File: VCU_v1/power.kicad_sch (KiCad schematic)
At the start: 0 parts

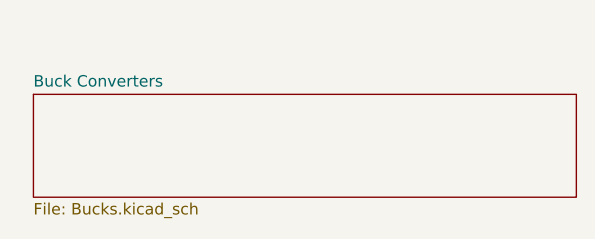
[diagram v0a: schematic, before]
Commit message: finished 12-5 buck
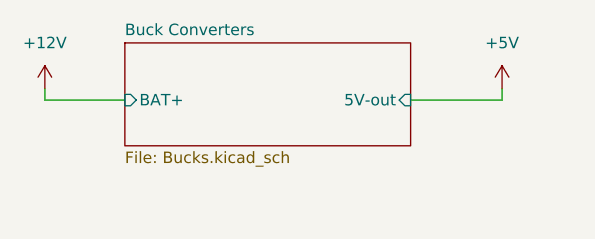
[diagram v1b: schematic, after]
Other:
- sheet Buck Converters ports: added 5V-out, BAT+; removed none
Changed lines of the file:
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@@
 	(generator_version "9.0")
 	(paper "A4")
-	(sheet
-		(at 102.87 51.435)
-		(size 60.325 11.43)
+	(wire
+		(pts
+			(xy 154.94 52.07) (xy 154.94 50.8)
+		)
+		(stroke
+			(width 0)
+			(type default)
+		)
+	)
+	(wire
+		(pts
+			(xy 144.78 52.07) (xy 154.94 52.07)
+		)
+		(stroke
+			(width 0)
+			(type default)
+		)
+	)
+	(wire
+		(pts
+			(xy 104.14 52.07) (xy 113.03 52.07)
+		)
+		(stroke
+			(width 0)
+			(type default)
+		)
+	)
+	(wire
+		(pts
+			(xy 104.14 50.8) (xy 104.14 52.07)
+		)
+		(stroke
+			(width 0)
+			(type default)
+		)
+	)
+	(symbol
+		(lib_id "power:+12V")
+		(at 104.14 50.8 0)
+		(unit 1)
 		(exclude_from_sim no)
 		(in_bom yes)
@@
 		(dnp no)
 		(fields_autoplaced yes)
+		(property "Reference" "#PWR09"
+			(at 104.14 54.61 0)
+			(effects
+				(font
+					(size 1.27 1.27)
+				)
+				(hide yes)
+			)
+		)
+		(property "Value" "+12V"
+			(at 104.14 45.72 0)
+			(effects
+				(font
+					(size 1.27 1.27)
+				)
+			)
+		)
+		(property "Footprint" ""
+			(at 104.14 50.8 0)
+			(effects
+				(font
+					(size 1.27 1.27)
+				)
+				(hide yes)
+			)
+		)
+		(property "Datasheet" ""
+			(at 104.14 50.8 0)
+			(effects
+				(font
+					(size 1.27 1.27)
+				)
+				(hide yes)
+			)
+		)
+		(property "Description" "Power symbol creates a global label with name \"+12V\""
+			(at 104.14 50.8 0)
+			(effects
+				(font
+					(size 1.27 1.27)
+				)
+				(hide yes)
+			)
+		)
+		(pin "1"
+		)
+		(instances
+			(project ""
+				(path "/4ee6c2ad-9a1b-4276-b3cf-1cc8dc52967e/9e4b5f8d-93dc-46d5-aa92-d0e0d2e07b3d"
+					(reference "#PWR09")
+					(unit 1)
+				)
+			)
+		)
+	)
+	(symbol
+		(lib_id "power:+5V")
+		(at 154.94 50.8 0)
+		(unit 1)
+		(exclude_from_sim no)
+		(in_bom yes)
+		(on_board yes)
+		(dnp no)
+		(fields_autoplaced yes)
+		(property "Reference" "#PWR010"
+			(at 154.94 54.61 0)
+			(effects
+				(font
+					(size 1.27 1.27)
+				)
+				(hide yes)
+			)
+		)
+		(property "Value" "+5V"
+			(at 154.94 45.72 0)
+			(effects
+				(font
+					(size 1.27 1.27)
+				)
+			)
+		)
+		(property "Footprint" ""
+			(at 154.94 50.8 0)
+			(effects
+				(font
+					(size 1.27 1.27)
+				)
+				(hide yes)
+			)
+		)
+		(property "Datasheet" ""
+			(at 154.94 50.8 0)
+			(effects
+				(font
+					(size 1.27 1.27)
+				)
+				(hide yes)
+			)
+		)
+		(property "Description" "Power symbol creates a global label with name \"+5V\""
+			(at 154.94 50.8 0)
+			(effects
+				(font
+					(size 1.27 1.27)
+				)
+				(hide yes)
+			)
+		)
+		(pin "1"
+		)
+		(instances
+			(project ""
+				(path "/4ee6c2ad-9a1b-4276-b3cf-1cc8dc52967e/9e4b5f8d-93dc-46d5-aa92-d0e0d2e07b3d"
+					(reference "#PWR010")
+					(unit 1)
+				)
+			)
+		)
+	)
+	(sheet
+		(at 113.03 45.72)
+		(size 31.75 11.43)
+		(exclude_from_sim no)
+		(in_bom yes)
+		(on_board yes)
+		(dnp no)
+		(fields_autoplaced yes)
 		(stroke
 			(width 0.1524)
@@
 		)
 		(property "Sheetname" "Buck Converters"
-			(at 102.87 50.7234 0)
+			(at 113.03 45.0084 0)
 			(effects
 				(font
@@
 		)
 		(property "Sheetfile" "Bucks.kicad_sch"
-			(at 102.87 63.4496 0)
+			(at 113.03 57.7346 0)
 			(effects
 				(font
@@
 			)
 		)
+		(pin "BAT+" input
+			(at 113.03 52.07 180)
+			(effects
+				(font
+					(size 1.27 1.27)
+				)
+				(justify left)
+			)
+		)
+		(pin "5V-out" input
+			(at 144.78 52.07 0)
+			(effects
+				(font
+					(size 1.27 1.27)
+				)
+				(justify right)
+			)
+		)

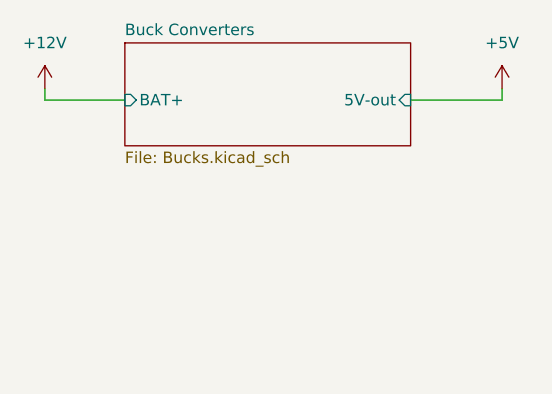
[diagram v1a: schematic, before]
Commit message: added STM, broke out communications I/Os for CAN, SPI, ADC
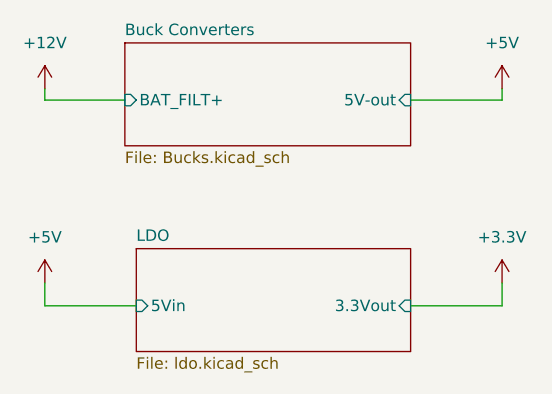
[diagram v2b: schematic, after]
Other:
- added sheet LDO (ldo.kicad_sch)
- sheet Buck Converters ports: added BAT_FILT+; removed BAT+
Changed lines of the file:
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@@
+	(wire
+		(pts
+			(xy 144.78 74.93) (xy 154.94 74.93)
+		)
+		(stroke
+			(width 0)
+			(type default)
+		)
+	)
+	(wire
+		(pts
+			(xy 104.14 72.39) (xy 104.14 74.93)
+		)
+		(stroke
+			(width 0)
+			(type default)
+		)
+	)
+	(wire
+		(pts
+			(xy 104.14 74.93) (xy 114.3 74.93)
+		)
+		(stroke
+			(width 0)
+			(type default)
+		)
+	)
+	(wire
+		(pts
+			(xy 154.94 74.93) (xy 154.94 72.39)
+		)
+		(stroke
+			(width 0)
+			(type default)
+		)
+	)
 	(wire
 		(pts
@@
 			(width 0)
 			(type default)
+		)
+	)
+	(symbol
+		(lib_id "power:+5V")
+		(at 104.14 72.39 0)
+		(unit 1)
+		(exclude_from_sim no)
+		(in_bom yes)
+		(on_board yes)
+		(dnp no)
+		(fields_autoplaced yes)
+		(property "Reference" "#PWR013"
+			(at 104.14 76.2 0)
+			(effects
+				(font
+					(size 1.27 1.27)
+				)
+				(hide yes)
+			)
+		)
+		(property "Value" "+5V"
+			(at 104.14 67.31 0)
+			(effects
+				(font
+					(size 1.27 1.27)
+				)
+			)
+		)
+		(property "Footprint" ""
+			(at 104.14 72.39 0)
+			(effects
+				(font
+					(size 1.27 1.27)
+				)
+				(hide yes)
+			)
+		)
+		(property "Datasheet" ""
+			(at 104.14 72.39 0)
+			(effects
+				(font
+					(size 1.27 1.27)
+				)
+				(hide yes)
+			)
+		)
+		(property "Description" "Power symbol creates a global label with name \"+5V\""
+			(at 104.14 72.39 0)
+			(effects
+				(font
+					(size 1.27 1.27)
+				)
+				(hide yes)
+			)
+		)
+		(pin "1"
+		)
+		(instances
+			(project ""
+				(path "/4ee6c2ad-9a1b-4276-b3cf-1cc8dc52967e/9e4b5f8d-93dc-46d5-aa92-d0e0d2e07b3d"
+					(reference "#PWR013")
+					(unit 1)
+				)
+			)
 		)
 	)
@@
 		)
 	)
+	(symbol
+		(lib_id "power:+3.3V")
+		(at 154.94 72.39 0)
+		(unit 1)
+		(exclude_from_sim no)
+		(in_bom yes)
+		(on_board yes)
+		(dnp no)
+		(fields_autoplaced yes)
+		(property "Reference" "#PWR014"
+			(at 154.94 76.2 0)
+			(effects
+				(font
+					(size 1.27 1.27)
+				)
+				(hide yes)
+			)
+		)
+		(property "Value" "+3.3V"
+			(at 154.94 67.31 0)
+			(effects
+				(font
+					(size 1.27 1.27)
+				)
+			)
+		)
+		(property "Footprint" ""
+			(at 154.94 72.39 0)
+			(effects
+				(font
+					(size 1.27 1.27)
+				)
+				(hide yes)
+			)
+		)
+		(property "Datasheet" ""
+			(at 154.94 72.39 0)
+			(effects
+				(font
+					(size 1.27 1.27)
+				)
+				(hide yes)
+			)
+		)
+		(property "Description" "Power symbol creates a global label with name \"+3.3V\""
+			(at 154.94 72.39 0)
+			(effects
+				(font
+					(size 1.27 1.27)
+				)
+				(hide yes)
+			)
+		)
+		(pin "1"
+		)
+		(instances
+			(project ""
+				(path "/4ee6c2ad-9a1b-4276-b3cf-1cc8dc52967e/9e4b5f8d-93dc-46d5-aa92-d0e0d2e07b3d"
+					(reference "#PWR014")
+					(unit 1)
+				)
+			)
+		)
+	)
+	(sheet
+		(at 114.3 68.58)
+		(size 30.48 11.43)
+		(exclude_from_sim no)
+		(in_bom yes)
+		(on_board yes)
+		(dnp no)
+		(fields_autoplaced yes)
+		(stroke
+			(width 0.1524)
+			(type solid)
+		)
+		(fill
+			(color 0 0 0 0.0000)
+		)
+		(property "Sheetname" "LDO"
+			(at 114.3 67.8684 0)
+			(effects
+				(font
+					(size 1.27 1.27)
+				)
+				(justify left bottom)
+			)
+		)
+		(property "Sheetfile" "ldo.kicad_sch"
+			(at 114.3 80.5946 0)
+			(effects
+				(font
+					(size 1.27 1.27)
+				)
+				(justify left top)
+			)
+		)
+		(pin "3.3Vout" input
+			(at 144.78 74.93 0)
+			(effects
+				(font
+					(size 1.27 1.27)
+				)
+				(justify right)
+			)
+		)
+		(pin "5Vin" input
+			(at 114.3 74.93 180)
+			(effects
+				(font
+					(size 1.27 1.27)
+				)
+				(justify left)
+			)
+		)
+		(instances
+			(project "VCU_v1"
+				(path "/4ee6c2ad-9a1b-4276-b3cf-1cc8dc52967e/9e4b5f8d-93dc-46d5-aa92-d0e0d2e07b3d"
+					(page "5")
+				)
+			)
+		)
+	)
 	(sheet
 		(at 113.03 45.72)
@@
 			)
 		)
-		(pin "BAT+" input
-			(at 113.03 52.07 180)
-			(effects
-				(font
-					(size 1.27 1.27)
-				)
-				(justify left)
-			)
-		)
 		(pin "5V-out" input
 			(at 144.78 52.07 0)
@@
 			)
 		)
+		(pin "BAT_FILT+" input
+			(at 113.03 52.07 180)
+			(effects
+				(font
+					(size 1.27 1.27)
+				)
+				(justify left)
+			)
+		)

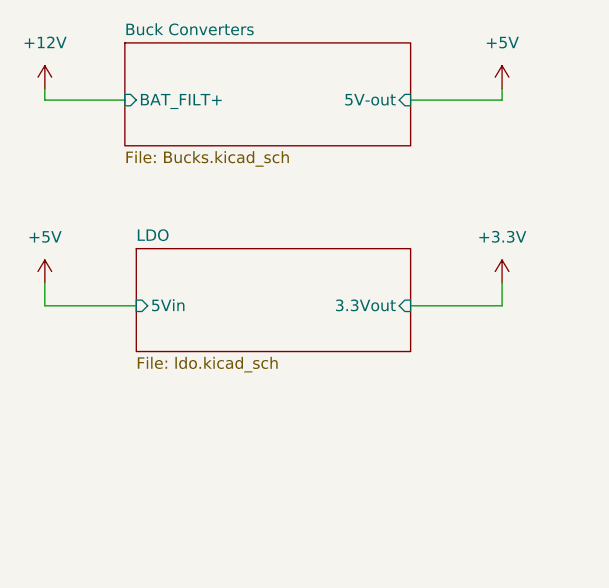
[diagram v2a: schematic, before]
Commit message: added rpp, pedal buffer/low pass, can transceivers, began connector pinout
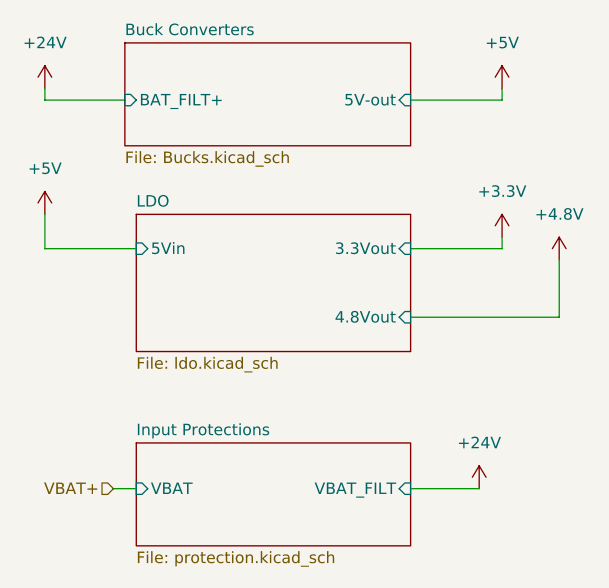
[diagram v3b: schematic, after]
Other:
- added sheet Input Protections (protection.kicad_sch)
- sheet LDO ports: added 4.8Vout; removed none

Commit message: p dih r
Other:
- sheet Buck Converters ports: added 20V-out; removed none
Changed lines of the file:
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@@
+	(wire
+		(pts
+			(xy 152.4 41.91) (xy 144.78 41.91)
+		)
+		(stroke
+			(width 0)
+			(type default)
+		)
+	)
 	(wire
 		(pts
@@
 		(pts
 			(xy 104.14 68.58) (xy 114.3 68.58)
+		)
+		(stroke
+			(width 0)
+			(type default)
+		)
+	)
+	(wire
+		(pts
+			(xy 152.4 38.1) (xy 152.4 41.91)
 		)
 		(stroke
@@
 	)
 	(symbol
+		(lib_id "power:VDD")
+		(at 152.4 38.1 0)
+		(unit 1)
+		(exclude_from_sim no)
+		(in_bom yes)
+		(on_board yes)
+		(dnp no)
+		(fields_autoplaced yes)
+		(property "Reference" "#PWR0101"
+			(at 152.4 41.91 0)
+			(effects
+				(font
+					(size 1.27 1.27)
+				)
+				(hide yes)
+			)
+		)
+		(property "Value" "20V-AMP"
+			(at 152.4 33.02 0)
+			(effects
+				(font
+					(size 1.27 1.27)
+				)
+			)
+		)
+		(property "Footprint" ""
+			(at 152.4 38.1 0)
+			(effects
+				(font
+					(size 1.27 1.27)
+				)
+				(hide yes)
+			)
+		)
+		(property "Datasheet" ""
+			(at 152.4 38.1 0)
+			(effects
+				(font
+					(size 1.27 1.27)
+				)
+				(hide yes)
+			)
+		)
+		(property "Description" "Power symbol creates a global label with name \"VDD\""
+			(at 152.4 38.1 0)
+			(effects
+				(font
+					(size 1.27 1.27)
+				)
+				(hide yes)
+			)
+		)
+		(pin "1"
+		)
+		(instances
+			(project ""
+				(path "/4ee6c2ad-9a1b-4276-b3cf-1cc8dc52967e/9e4b5f8d-93dc-46d5-aa92-d0e0d2e07b3d"
+					(reference "#PWR0101")
+					(unit 1)
+				)
+			)
+		)
+	)
+	(symbol
 		(lib_id "power:+24V")
 		(at 104.14 50.8 0)
@@
 	)
 	(sheet
-		(at 113.03 45.72)
-		(size 31.75 11.43)
+		(at 113.03 34.29)
+		(size 31.75 22.86)
 		(exclude_from_sim no)
 		(in_bom yes)
@@
 		)
 		(property "Sheetname" "Buck Converters"
-			(at 113.03 45.0084 0)
+			(at 113.03 33.5784 0)
 			(effects
 				(font
@@
 			)
 		)
+		(pin "20V-out" input
+			(at 144.78 41.91 0)
+			(effects
+				(font
+					(size 1.27 1.27)
+				)
+				(justify right)
+			)
+		)

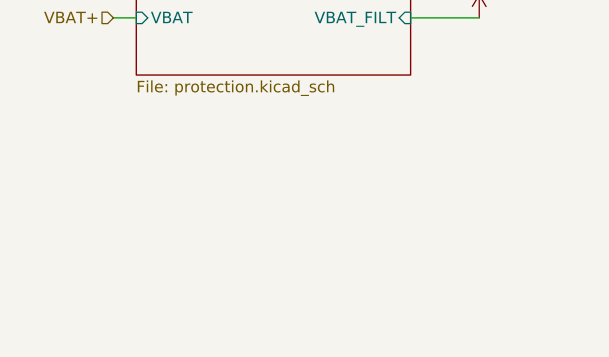
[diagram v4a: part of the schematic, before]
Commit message: v1 schematic (actually) complete, let the layout commence
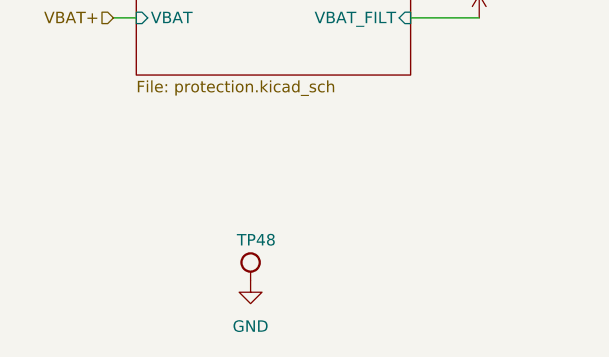
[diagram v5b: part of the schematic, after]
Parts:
- added TP48: RH-5015, TestPoint:TestPoint_Keystone_5015_Micro_Mini, symbol .Test-Point:RH-5015
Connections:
- new net GND: TP48.1
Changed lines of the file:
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@@
+	)
+	(symbol
+		(lib_id "power:GND")
+		(at 127 124.46 0)
+		(unit 1)
+		(exclude_from_sim no)
+		(in_bom yes)
+		(on_board yes)
+		(dnp no)
+		(fields_autoplaced yes)
+		(property "Reference" "#PWR0144"
+			(at 127 130.81 0)
+			(effects
+				(font
+					(size 1.27 1.27)
+				)
+				(hide yes)
+			)
+		)
+		(property "Value" "GND"
+			(at 127 129.54 0)
+			(effects
+				(font
+					(size 1.27 1.27)
+				)
+			)
+		)
+		(property "Footprint" ""
+			(at 127 124.46 0)
+			(effects
+				(font
+					(size 1.27 1.27)
+				)
+				(hide yes)
+			)
+		)
+		(property "Datasheet" ""
+			(at 127 124.46 0)
+			(effects
+				(font
+					(size 1.27 1.27)
+				)
+				(hide yes)
+			)
+		)
+		(property "Description" "Power symbol creates a global label with name \"GND\" , ground"
+			(at 127 124.46 0)
+			(effects
+				(font
+					(size 1.27 1.27)
+				)
+				(hide yes)
+			)
+		)
+		(pin "1"
+		)
+		(instances
+			(project ""
+				(path "/4ee6c2ad-9a1b-4276-b3cf-1cc8dc52967e/9e4b5f8d-93dc-46d5-aa92-d0e0d2e07b3d"
+					(reference "#PWR0144")
+					(unit 1)
+				)
+			)
+		)
 	)
 	(symbol
@@
 		(dnp no)
 		(fields_autoplaced yes)
-		(property "Reference" "#PWR013"
+		(property "Reference" "#PWR04"
 			(at 104.14 68.58 0)
 			(effects
@@
 			(project ""
 				(path "/4ee6c2ad-9a1b-4276-b3cf-1cc8dc52967e/9e4b5f8d-93dc-46d5-aa92-d0e0d2e07b3d"
-					(reference "#PWR013")
+					(reference "#PWR04")
 					(unit 1)
 				)
@@
 		(dnp no)
 		(fields_autoplaced yes)
-		(property "Reference" "#PWR0101"
+		(property "Reference" "#PWR05"
 			(at 152.4 41.91 0)
 			(effects
@@
 			(project ""
 				(path "/4ee6c2ad-9a1b-4276-b3cf-1cc8dc52967e/9e4b5f8d-93dc-46d5-aa92-d0e0d2e07b3d"
-					(reference "#PWR0101")
+					(reference "#PWR05")
 					(unit 1)
 				)
@@
 		(dnp no)
 		(fields_autoplaced yes)
-		(property "Reference" "#PWR09"
+		(property "Reference" "#PWR03"
 			(at 104.14 54.61 0)
 			(effects
@@
 			(project ""
 				(path "/4ee6c2ad-9a1b-4276-b3cf-1cc8dc52967e/9e4b5f8d-93dc-46d5-aa92-d0e0d2e07b3d"
-					(reference "#PWR09")
+					(reference "#PWR03")
+					(unit 1)
+				)
+			)
+		)
+	)
+	(symbol
+		(lib_id ".Test-Point:RH-5015")
+		(at 127 124.46 0)
+		(unit 1)
+		(exclude_from_sim no)
+		(in_bom yes)
+		(on_board yes)
+		(dnp no)
+		(property "Reference" "TP48"
+			(at 125.4768 119.2037 0)
+			(effects
+				(font
+					(size 1.27 1.27)
+				)
+				(justify left top)
+			)
+		)
+		(property "Value" "RH-5015"
+			(at 125.4768 117.0535 0)
+			(effects
+				(font
+					(size 1.27 1.27)
+				)
+				(justify left top)
+				(hide yes)
+			)
+		)
+		(property "Footprint" "TestPoint:TestPoint_Keystone_5015_Micro_Mini"
+			(at 127 135.89 0)
+			(effects
+				(font
+					(size 1.27 1.27)
+				)
+				(justify left bottom)
+				(hide yes)
+			)
+		)
+		(property "Datasheet" "https://wmsc.lcsc.com/wmsc/upload/file/pdf/v2/lcsc/2310260935_ronghe-RH-5015_C5199798.pdf"
+			(at 127 139.7 0)
+			(effects
+				(font
+					(size 1.27 1.27)
+				)
+				(justify left bottom)
+				(hide yes)
+			)
+		)
+		(property "Description" "Surface-mount grabby test point"
+			(at 127 143.51 0)
+			(effects
+				(font
+					(size 1.27 1.27)
+				)
+				(justify left bottom)
+				(hide yes)
+			)
+		)
+		(property "Link" "https://jlcpcb.com/partdetail/Ronghe-RH5015/C5199798"
+			(at 127 147.32 0)
+			(effects
+				(font
+					(size 1.27 1.27)
+				)
+				(justify left bottom)
+				(hide yes)
+			)
+		)
+		(property "Digikey P/N" "36-5015CT-ND"
+			(at 127 158.75 0)
+			(effects
+				(font
+					(size 1.27 1.27)
+				)
+				(justify left bottom)
+				(hide yes)
+			)
+		)
+		(property "Mouser P/N" "534-5015"
+			(at 127 162.56 0)
+			(effects
+				(font
+					(size 1.27 1.27)
+				)
+				(justify left bottom)
+				(hide yes)
+			)
+		)
+		(property "LCSC P/N" "C5199798"
+			(at 127 166.37 0)
+			(effects
+				(font
+					(size 1.27 1.27)
+				)
+				(justify left bottom)
+				(hide yes)
+			)
+		)
+		(property "Manufacturer" "Ronghe"
+			(at 127 151.13 0)
+			(effects
+				(font
+					(size 1.27 1.27)
+				)
+				(justify left bottom)
+				(hide yes)
+			)
+		)
+		(property "Manufacturer P/N" "RH-5015"
+			(at 127 154.94 0)
+			(effects
+				(font
+					(size 1.27 1.27)
+				)
+				(justify left bottom)
+				(hide yes)
+			)
+		)
+		(property "LCSC Part #" "C5199798"
+			(at 127 124.46 0)
+			(effects
+				(font
+					(size 1.27 1.27)
+				)
+				(hide yes)
+			)
+		)
+		(pin "1"
+		)
+		(instances
+			(project "VCU_v1"
+				(path "/4ee6c2ad-9a1b-4276-b3cf-1cc8dc52967e/9e4b5f8d-93dc-46d5-aa92-d0e0d2e07b3d"
+					(reference "TP48")
 					(unit 1)
 				)
@@
 		(dnp no)
 		(fields_autoplaced yes)
-		(property "Reference" "#PWR033"
+		(property "Reference" "#PWR09"
 			(at 161.29 73.66 0)
 			(effects
@@
 			(project ""
 				(path "/4ee6c2ad-9a1b-4276-b3cf-1cc8dc52967e/9e4b5f8d-93dc-46d5-aa92-d0e0d2e07b3d"
-					(reference "#PWR033")
+					(reference "#PWR09")
 					(unit 1)
 				)
@@
 		(dnp no)
 		(fields_autoplaced yes)
-		(property "Reference" "#PWR028"
+		(property "Reference" "#PWR06"
 			(at 152.4 99.06 0)
 			(effects
@@
 			(project "VCU_v1"
 				(path "/4ee6c2ad-9a1b-4276-b3cf-1cc8dc52967e/9e4b5f8d-93dc-46d5-aa92-d0e0d2e07b3d"
-					(reference "#PWR028")
+					(reference "#PWR06")
 					(unit 1)
 				)
@@
 		(dnp no)
 		(fields_autoplaced yes)
-		(property "Reference" "#PWR010"
+		(property "Reference" "#PWR07"
 			(at 154.94 54.61 0)
 			(effects
@@
 			(project ""
 				(path "/4ee6c2ad-9a1b-4276-b3cf-1cc8dc52967e/9e4b5f8d-93dc-46d5-aa92-d0e0d2e07b3d"
-					(reference "#PWR010")
+					(reference "#PWR07")
 					(unit 1)
 				)
@@
 		(dnp no)
 		(fields_autoplaced yes)
-		(property "Reference" "#PWR014"
+		(property "Reference" "#PWR08"
 			(at 154.94 71.12 0)
 			(effects
@@
 			(project ""
 				(path "/4ee6c2ad-9a1b-4276-b3cf-1cc8dc52967e/9e4b5f8d-93dc-46d5-aa92-d0e0d2e07b3d"
-					(reference "#PWR014")
-					(unit 1)
-				)
+					(reference "#PWR08")
+					(unit 1)
+				)

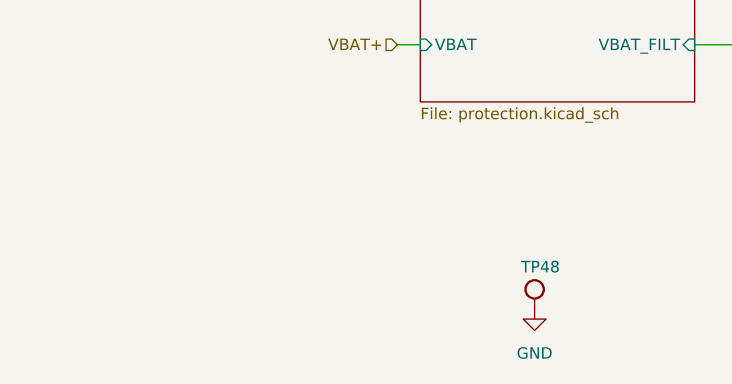
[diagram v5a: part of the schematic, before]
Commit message: i lied i had to add gnd test points
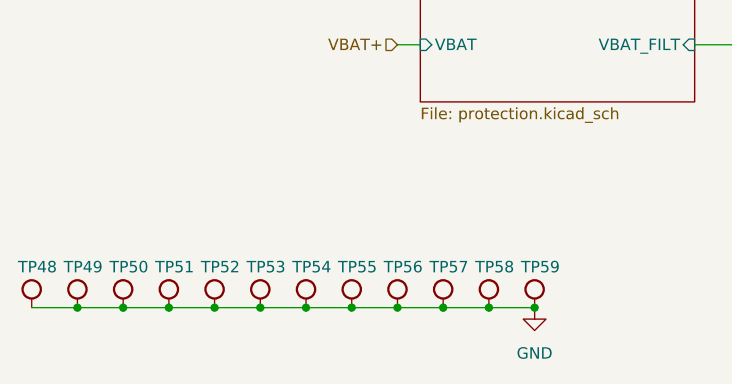
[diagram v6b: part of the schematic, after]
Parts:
- added TP49, TP50, TP51, TP52, TP53, TP54, TP55, TP56, TP57, TP58, TP59: RH-5015, TestPoint:TestPoint_Keystone_5015_Micro_Mini, symbol .Test-Point:RH-5015
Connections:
- net GND: now also TP49.1, TP50.1, TP51.1, TP52.1, TP53.1, TP54.1, TP55.1, TP56.1, TP57.1, TP58.1, TP59.1
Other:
- moved on the sheet: TP48
